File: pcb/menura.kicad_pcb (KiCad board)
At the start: 2 copper layers, 128.4 x 108.5 mm, 53 parts, among them SW1 SW_Push, SW10 SW_Push, SW11 SW_Push, SW12 SW_Push, SW13 SW_Push, SW14 SW_Push, SW15 SW_Push, SW16 SW_Push, SW17 SW_Push, SW18 SW_Push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

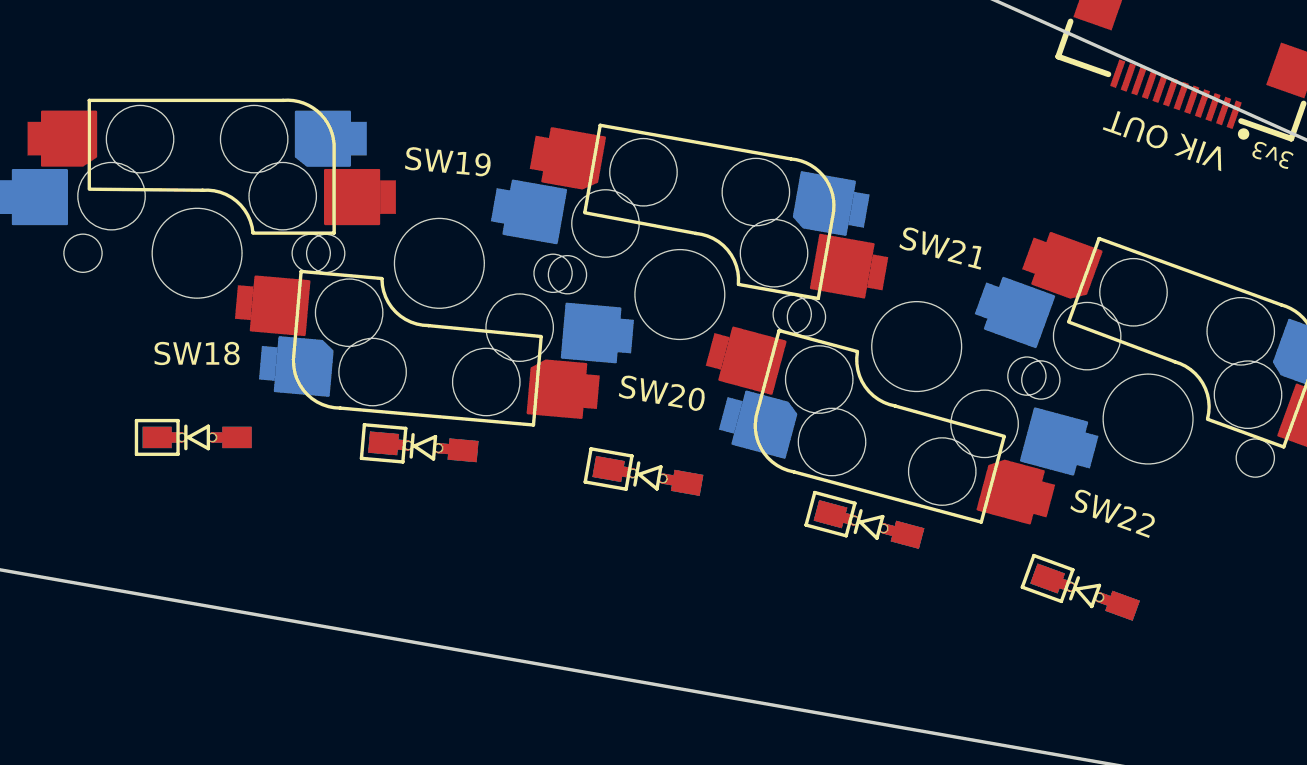
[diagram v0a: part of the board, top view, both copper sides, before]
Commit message: fix diode ordering
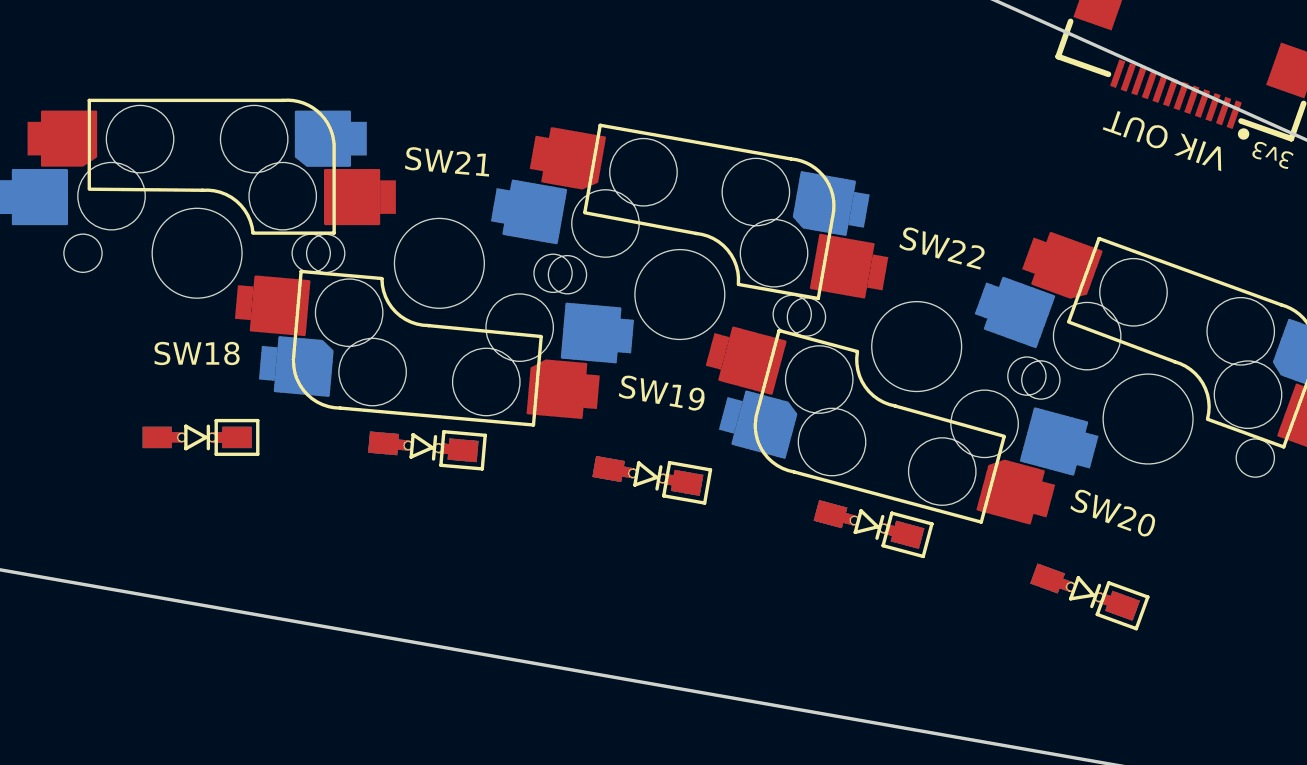
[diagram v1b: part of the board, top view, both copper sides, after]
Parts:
- moved SW21 21.6 mm to (167.8, 117.0), turned to 175 degrees
- moved SW20 21.6 mm to (199.3, 123.9), turned to -20 degrees
- moved SW19 10.8 mm to (178.5, 118.3), turned to -10 degrees
- moved SW22 10.8 mm to (189.0, 120.7), turned to 165 degrees
- turned D18 to 180 degrees
- turned D19 to 170 degrees
- turned D20 to 160 degrees
- turned D21 to 175 degrees
- turned D22 to 165 degrees
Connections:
- SW19 pad 1: col2 -> col3
- SW20 pad 1: col3 -> col4
- SW21 pad 1: col3 -> col2
- SW22 pad 1: col4 -> col3

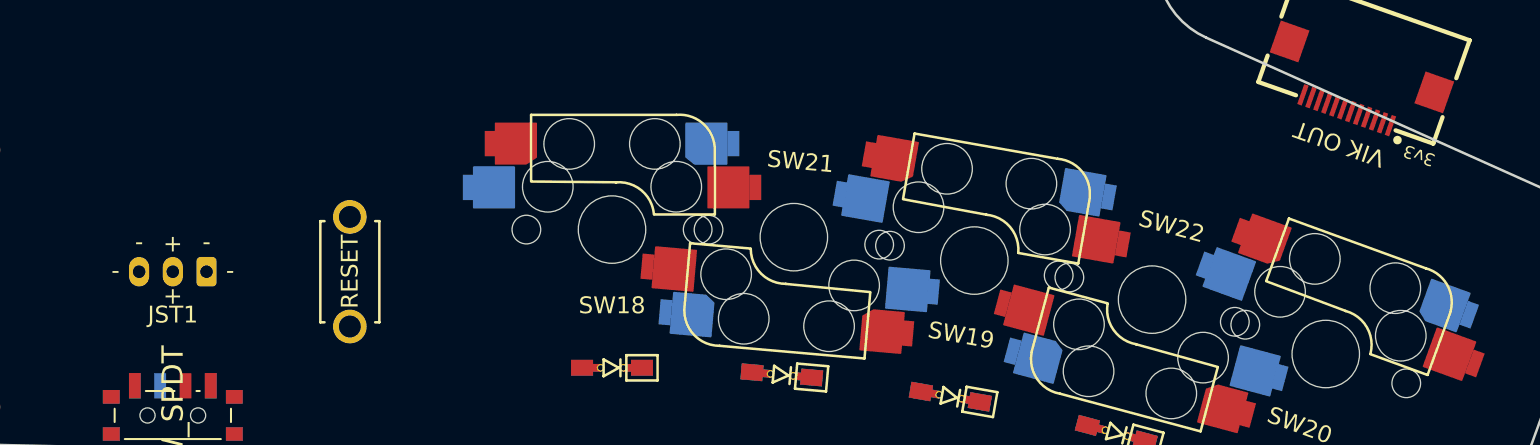
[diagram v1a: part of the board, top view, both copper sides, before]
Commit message: update footprints: centering, pad assignments
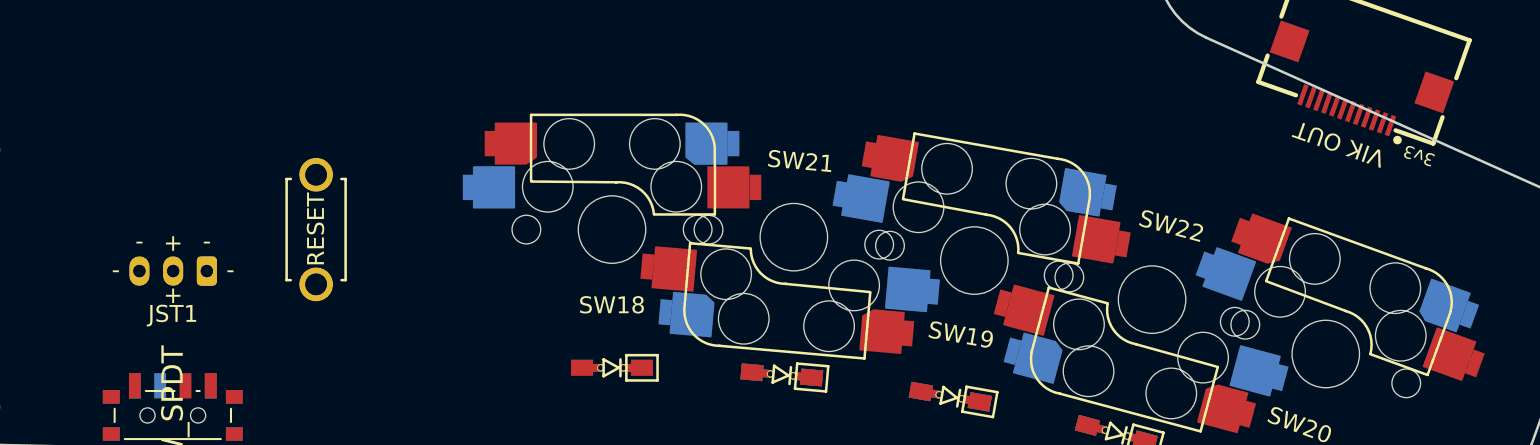
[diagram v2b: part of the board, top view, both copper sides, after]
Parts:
- moved JST1 3.20 mm to (130.9, 116.5)
- moved RSW1 3.20 mm to (139.4, 116.5)
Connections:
- MCU1 pad 10: col0 -> CS
- MCU1 pad 11: col1 -> col4
- MCU1 pad 12: col2 -> row3
- MCU1 pad 13: CS -> col3
- MCU1 pad 14: MOSI -> col2
- MCU1 pad 15: MISO -> col1
- MCU1 pad 16: SCLK -> col0
- MCU1 pad 19: col4 -> row2
- MCU1 pad 20: col3 -> row1
- MCU1 pad 7: row1 -> SCLK
- MCU1 pad 8: row2 -> MISO
- MCU1 pad 9: row3 -> MOSI

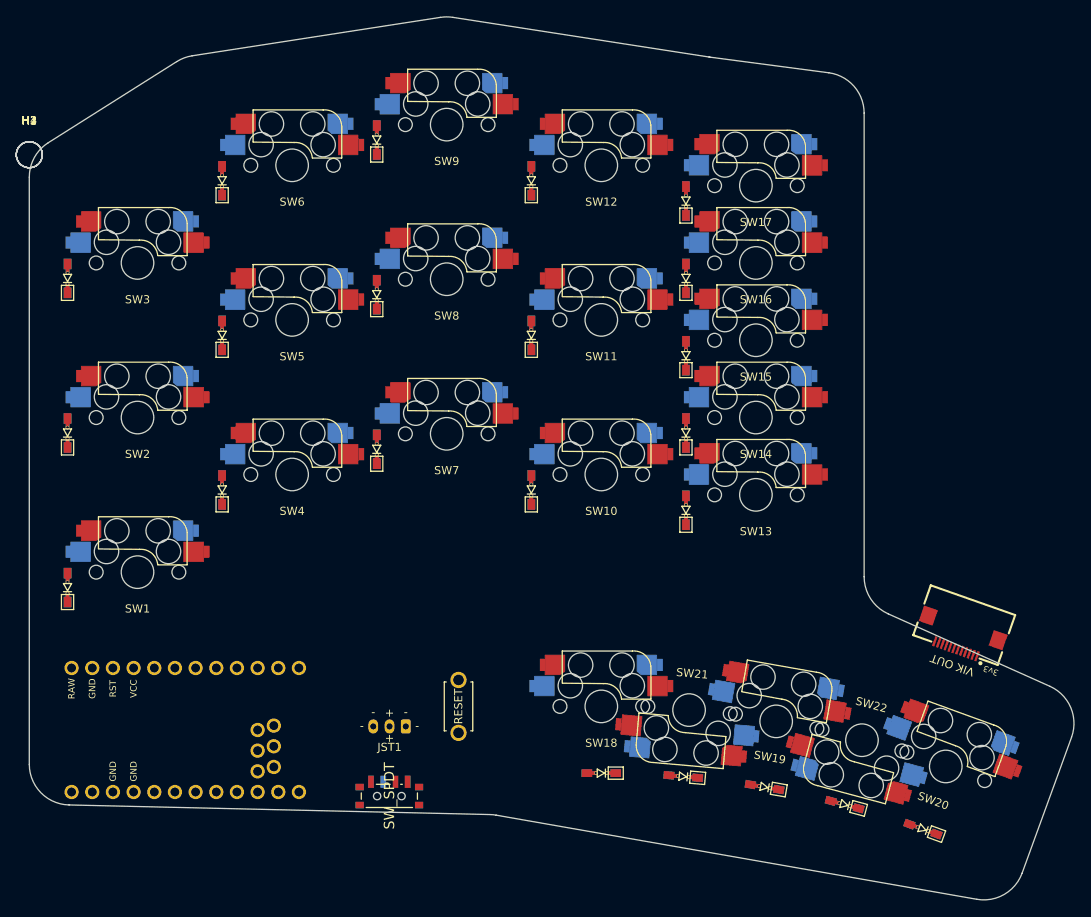
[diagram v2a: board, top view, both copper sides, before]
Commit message: iterate on power switch and jst placement
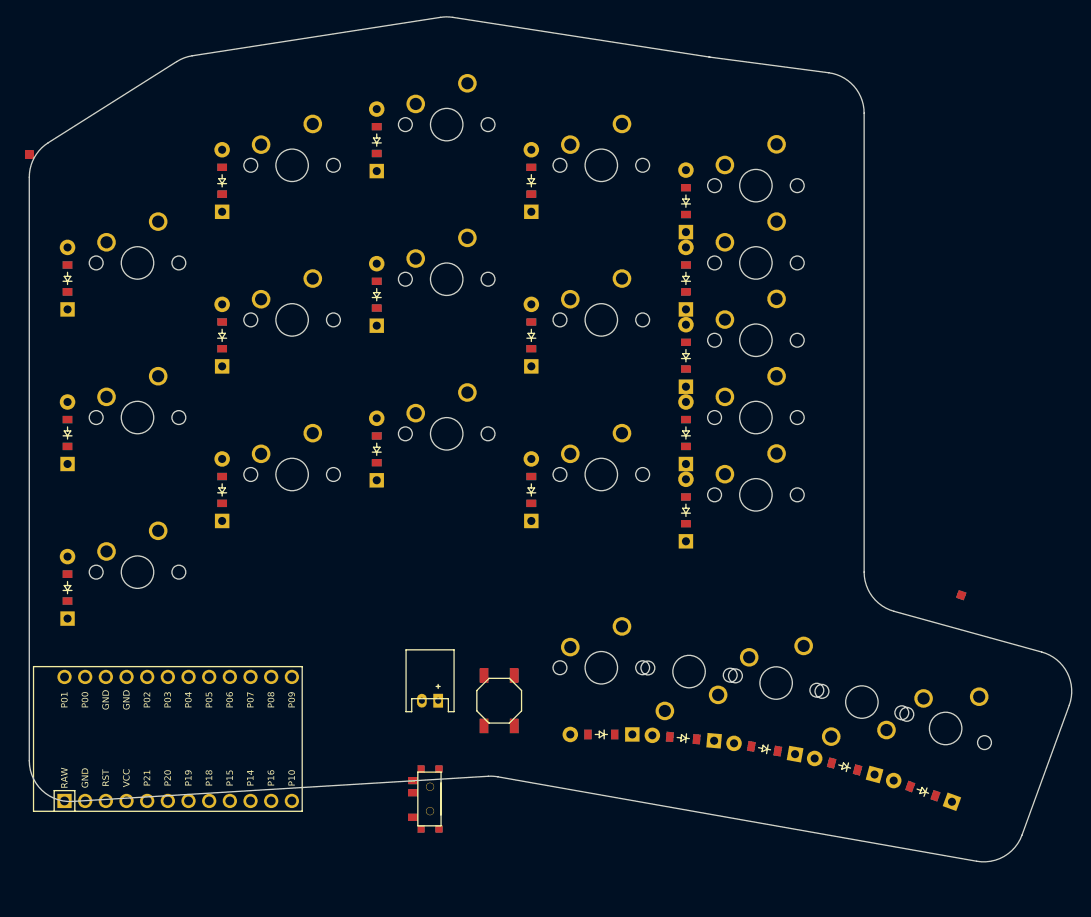
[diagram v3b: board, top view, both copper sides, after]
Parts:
- D1, D10, D11, D12, D13, D14, D15, D16, D17, D18, D19, D2, D20, D21, D22, D3, D4, D5, D6, D7, D8, D9: value 1N4148W -> (none); footprint quappo:Diode_SMD-reversible-urchin -> ComboDiode
- H1, H2, H3, H4: value MountingHole -> (none); footprint MountingHole:MountingHole_3.2mm_M3 -> SMDPad
- JST1: value Conn_01x03_Socket -> (none); footprint quappo:Connector_JST-PH-3prong -> JST_PH_S2B-PH-K_02x2.00mm_Angled
- MCU1: value N!N -> (none); footprint quappo:MCU_nice-nano -> ProMicro
- PWR1: value SW_SPDT -> (none); footprint quappo:Switch_power-reversible-kim -> E73:SPDT_C128955
- RSW1: value SW_Push -> (none); footprint quappo:Switch_reset-2pin -> E73:SW_TACT_ALPS_SKQGABE010
- SW1, SW10, SW11, SW12, SW13, SW14, SW15, SW16, SW17, SW18, SW19, SW2, SW20, SW21, SW22, SW3, SW4, SW5, SW6, SW7, SW8, SW9: value SW_Push -> (none); footprint quappo:Switch_MX-hotswap-reversible -> MX
- VIK1: value ~ -> (none); footprint quappo:Connector_vik-keyboard-horizontal -> SMDPad
- moved JST1 5.05 mm to (135.9, 115.8)
- moved RSW1 5.05 mm to (144.4, 115.8)
- moved PWR1 5.01 mm to (135.9, 127.9)
- moved D18 4.75 mm to (157.0, 120.0)
- moved SW18 4.75 mm to (157.0, 111.8)
- moved D21 4.73 mm to (167.1, 120.4)
- moved SW21 4.73 mm to (167.8, 112.2)
- moved SW19 4.71 mm to (178.5, 113.6)
- moved D19 4.71 mm to (177.1, 121.7)
- moved D22 4.69 mm to (186.9, 123.9)
- moved SW22 4.69 mm to (189.0, 116.0)
- moved VIK1 4.67 mm to (201.2, 102.8)
- moved SW20 4.67 mm to (199.3, 119.2)
- moved D20 4.67 mm to (196.5, 126.9)
- moved MCU1 1.50 mm to (105.0, 120.5)
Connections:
- D1 pad 1: row2 -> (no net)
- D1 pad 2: Net-(D1-A) -> (no net)
- D10 pad 1: row2 -> (no net)
- D10 pad 2: Net-(D10-A) -> (no net)
- D11 pad 1: row1 -> (no net)
- D11 pad 2: Net-(D11-A) -> (no net)
- D12 pad 1: row0 -> (no net)
- D12 pad 2: Net-(D12-A) -> (no net)
- D13 pad 1: row2 -> (no net)
- D13 pad 2: Net-(D13-A) -> (no net)
- D14 pad 1: row1 -> (no net)
- D14 pad 2: Net-(D14-A) -> (no net)
- D15 pad 1: row1 -> (no net)
- D15 pad 2: Net-(D15-A) -> (no net)
- D16 pad 1: row0 -> (no net)
- D16 pad 2: Net-(D16-A) -> (no net)
- D17 pad 1: row0 -> (no net)
- D17 pad 2: Net-(D17-A) -> (no net)
- D18 pad 1: row3 -> (no net)
- D18 pad 2: Net-(D18-A) -> (no net)
- D19 pad 1: row3 -> (no net)
- D19 pad 2: Net-(D19-A) -> (no net)
- D2 pad 1: row1 -> (no net)
- D2 pad 2: Net-(D2-A) -> (no net)
- D20 pad 1: row3 -> (no net)
- D20 pad 2: Net-(D20-A) -> (no net)
- D21 pad 1: row3 -> (no net)
- D21 pad 2: Net-(D21-A) -> (no net)
- D22 pad 1: row3 -> (no net)
- D22 pad 2: Net-(D22-A) -> (no net)
- D3 pad 1: row0 -> (no net)
- D3 pad 2: Net-(D3-A) -> (no net)
- D4 pad 1: row2 -> (no net)
- D4 pad 2: Net-(D4-A) -> (no net)
- D5 pad 1: row1 -> (no net)
- D5 pad 2: Net-(D5-A) -> (no net)
- D6 pad 1: row0 -> (no net)
- D6 pad 2: Net-(D6-A) -> (no net)
- D7 pad 1: row2 -> (no net)
- D7 pad 2: Net-(D7-A) -> (no net)
- D8 pad 1: row1 -> (no net)
- D8 pad 2: Net-(D8-A) -> (no net)
- D9 pad 1: row0 -> (no net)
- D9 pad 2: Net-(D9-A) -> (no net)
- JST1 pad 1: GND -> (no net)
- JST1 pad 2: Net-(JST1-Pin_2) -> (no net)
- MCU1 pad 1: unconnected-(MCU1-006-Pad1) -> RAW
- MCU1 pad 10: CS -> P14
- MCU1 pad 11: col4 -> P16
- MCU1 pad 12: row3 -> P10
- MCU1 pad 13: col3 -> P1
- MCU1 pad 14: col2 -> P0
- MCU1 pad 15: col1 -> GND
- MCU1 pad 16: col0 -> GND
- MCU1 pad 17: VIK_GPIO2 -> P2
- MCU1 pad 18: VIK_GPIO1 -> P3
- MCU1 pad 19: row2 -> P4
- MCU1 pad 2: row0 -> GND
- MCU1 pad 20: row1 -> P5
- MCU1 pad 21: +3.3V -> P6
- MCU1 pad 22: RST -> P7
- MCU1 pad 23: GND -> P8
- MCU1 pad 24: RAW -> P9
- MCU1 pad 3: GND -> RST
- MCU1 pad 4: GND -> VCC
- MCU1 pad 5: SDA -> P21
- MCU1 pad 6: SCL -> P20
- MCU1 pad 7: SCLK -> P19
- MCU1 pad 8: MISO -> P18
- MCU1 pad 9: MOSI -> P15
- PWR1 pad 1: RAW -> (no net)
- PWR1 pad 2: Net-(JST1-Pin_2) -> (no net)
- PWR1 pad 3: unconnected-(PWR1-C-Pad3)_0 -> (no net)
- RSW1 pad 1: GND -> (no net)
- RSW1 pad 2: RST -> (no net)
- SW1 pad 1: col0 -> (no net)
- SW1 pad 2: Net-(D1-A) -> (no net)
- SW10 pad 1: col3 -> (no net)
- SW10 pad 2: Net-(D10-A) -> (no net)
- SW11 pad 1: col3 -> (no net)
- SW11 pad 2: Net-(D11-A) -> (no net)
- SW12 pad 1: col3 -> (no net)
- SW12 pad 2: Net-(D12-A) -> (no net)
- SW13 pad 1: col4 -> (no net)
- SW13 pad 2: Net-(D13-A) -> (no net)
- SW14 pad 1: col4 -> (no net)
- SW14 pad 2: Net-(D14-A) -> (no net)
- SW15 pad 1: col4 -> (no net)
- SW15 pad 2: Net-(D15-A) -> (no net)
- SW16 pad 1: col4 -> (no net)
- SW16 pad 2: Net-(D16-A) -> (no net)
- SW17 pad 1: col4 -> (no net)
- SW17 pad 2: Net-(D17-A) -> (no net)
- SW18 pad 1: col2 -> (no net)
- SW18 pad 2: Net-(D18-A) -> (no net)
- SW19 pad 1: col3 -> (no net)
- SW19 pad 2: Net-(D19-A) -> (no net)
- SW2 pad 1: col0 -> (no net)
- SW2 pad 2: Net-(D2-A) -> (no net)
- SW20 pad 1: col4 -> (no net)
- SW20 pad 2: Net-(D20-A) -> (no net)
- SW21 pad 1: col2 -> (no net)
- SW21 pad 2: Net-(D21-A) -> (no net)
- SW22 pad 1: col3 -> (no net)
- SW22 pad 2: Net-(D22-A) -> (no net)
- SW3 pad 1: col0 -> (no net)
- SW3 pad 2: Net-(D3-A) -> (no net)
- SW4 pad 1: col1 -> (no net)
- SW4 pad 2: Net-(D4-A) -> (no net)
- SW5 pad 1: col1 -> (no net)
- SW5 pad 2: Net-(D5-A) -> (no net)
- SW6 pad 1: col1 -> (no net)
- SW6 pad 2: Net-(D6-A) -> (no net)
- SW7 pad 1: col2 -> (no net)
- SW7 pad 2: Net-(D7-A) -> (no net)
- SW8 pad 1: col2 -> (no net)
- SW8 pad 2: Net-(D8-A) -> (no net)
- SW9 pad 1: col2 -> (no net)
- SW9 pad 2: Net-(D9-A) -> (no net)
- VIK1 pad 1: +3.3V -> (no net)
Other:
- board size 128.4 x 108.5 mm -> 128.1 x 103.8 mm
- net class Default added: clearance 0.2, trace_width 0.25, via_dia 0.8, via_drill 0.4

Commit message: iterate on vik placement
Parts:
- D1, D10, D11, D12, D13, D14, D15, D16, D17, D18, D19, D2, D20, D21, D22, D3, D4, D5, D6, D7, D8, D9: value (none) -> 1N4148W; footprint ComboDiode -> quappo:Diode_SMD-reversible-urchin
- H1, H2, H3, H4: value (none) -> MountingHole; footprint SMDPad -> MountingHole:MountingHole_3.2mm_M3
- JST1: value (none) -> Conn_01x03_Socket; footprint JST_PH_S2B-PH-K_02x2.00mm_Angled -> quappo:Connector_JST-PH-3prong
- MCU1: value (none) -> N!N; footprint ProMicro -> quappo:MCU_nice-nano
- PWR1: value (none) -> SW_SPDT; footprint E73:SPDT_C128955 -> quappo:Switch_power-reversible-kim
- RSW1: value (none) -> SW_Push; footprint E73:SW_TACT_ALPS_SKQGABE010 -> quappo:Switch_reset-2pin
- SW1, SW10, SW11, SW12, SW13, SW14, SW15, SW16, SW17, SW18, SW19, SW2, SW20, SW21, SW22, SW3, SW4, SW5, SW6, SW7, SW8, SW9: value (none) -> SW_Push; footprint MX -> quappo:Switch_MX-hotswap-reversible
- VIK1: value (none) -> ~; footprint SMDPad -> quappo:Connector_vik-keyboard-horizontal
- moved VIK1 8.59 mm to (192.7, 102.4), turned to 165 degrees
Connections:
- D1 pad 1: (no net) -> row2
- D1 pad 2: (no net) -> Net-(D1-A)
- D10 pad 1: (no net) -> row2
- D10 pad 2: (no net) -> Net-(D10-A)
- D11 pad 1: (no net) -> row1
- D11 pad 2: (no net) -> Net-(D11-A)
- D12 pad 1: (no net) -> row0
- D12 pad 2: (no net) -> Net-(D12-A)
- D13 pad 1: (no net) -> row2
- D13 pad 2: (no net) -> Net-(D13-A)
- D14 pad 1: (no net) -> row1
- D14 pad 2: (no net) -> Net-(D14-A)
- D15 pad 1: (no net) -> row1
- D15 pad 2: (no net) -> Net-(D15-A)
- D16 pad 1: (no net) -> row0
- D16 pad 2: (no net) -> Net-(D16-A)
- D17 pad 1: (no net) -> row0
- D17 pad 2: (no net) -> Net-(D17-A)
- D18 pad 1: (no net) -> row3
- D18 pad 2: (no net) -> Net-(D18-A)
- D19 pad 1: (no net) -> row3
- D19 pad 2: (no net) -> Net-(D19-A)
- D2 pad 1: (no net) -> row1
- D2 pad 2: (no net) -> Net-(D2-A)
- D20 pad 1: (no net) -> row3
- D20 pad 2: (no net) -> Net-(D20-A)
- D21 pad 1: (no net) -> row3
- D21 pad 2: (no net) -> Net-(D21-A)
- D22 pad 1: (no net) -> row3
- D22 pad 2: (no net) -> Net-(D22-A)
- D3 pad 1: (no net) -> row0
- D3 pad 2: (no net) -> Net-(D3-A)
- D4 pad 1: (no net) -> row2
- D4 pad 2: (no net) -> Net-(D4-A)
- D5 pad 1: (no net) -> row1
- D5 pad 2: (no net) -> Net-(D5-A)
- D6 pad 1: (no net) -> row0
- D6 pad 2: (no net) -> Net-(D6-A)
- D7 pad 1: (no net) -> row2
- D7 pad 2: (no net) -> Net-(D7-A)
- D8 pad 1: (no net) -> row1
- D8 pad 2: (no net) -> Net-(D8-A)
- D9 pad 1: (no net) -> row0
- D9 pad 2: (no net) -> Net-(D9-A)
- JST1 pad 1: (no net) -> GND
- JST1 pad 2: (no net) -> Net-(JST1-Pin_2)
- MCU1 pad 1: RAW -> unconnected-(MCU1-006-Pad1)
- MCU1 pad 10: P14 -> CS
- MCU1 pad 11: P16 -> col4
- MCU1 pad 12: P10 -> row3
- MCU1 pad 13: P1 -> col3
- MCU1 pad 14: P0 -> col2
- MCU1 pad 15: GND -> col1
- MCU1 pad 16: GND -> col0
- MCU1 pad 17: P2 -> VIK_GPIO2
- MCU1 pad 18: P3 -> VIK_GPIO1
- MCU1 pad 19: P4 -> row2
- MCU1 pad 2: GND -> row0
- MCU1 pad 20: P5 -> row1
- MCU1 pad 21: P6 -> +3.3V
- MCU1 pad 22: P7 -> RST
- MCU1 pad 23: P8 -> GND
- MCU1 pad 24: P9 -> RAW
- MCU1 pad 3: RST -> GND
- MCU1 pad 4: VCC -> GND
- MCU1 pad 5: P21 -> SDA
- MCU1 pad 6: P20 -> SCL
- MCU1 pad 7: P19 -> SCLK
- MCU1 pad 8: P18 -> MISO
- MCU1 pad 9: P15 -> MOSI
- PWR1 pad 1: (no net) -> RAW
- PWR1 pad 2: (no net) -> Net-(JST1-Pin_2)
- PWR1 pad 3: (no net) -> unconnected-(PWR1-C-Pad3)_0
- RSW1 pad 1: (no net) -> GND
- RSW1 pad 2: (no net) -> RST
- SW1 pad 1: (no net) -> col0
- SW1 pad 2: (no net) -> Net-(D1-A)
- SW10 pad 1: (no net) -> col3
- SW10 pad 2: (no net) -> Net-(D10-A)
- SW11 pad 1: (no net) -> col3
- SW11 pad 2: (no net) -> Net-(D11-A)
- SW12 pad 1: (no net) -> col3
- SW12 pad 2: (no net) -> Net-(D12-A)
- SW13 pad 1: (no net) -> col4
- SW13 pad 2: (no net) -> Net-(D13-A)
- SW14 pad 1: (no net) -> col4
- SW14 pad 2: (no net) -> Net-(D14-A)
- SW15 pad 1: (no net) -> col4
- SW15 pad 2: (no net) -> Net-(D15-A)
- SW16 pad 1: (no net) -> col4
- SW16 pad 2: (no net) -> Net-(D16-A)
- SW17 pad 1: (no net) -> col4
- SW17 pad 2: (no net) -> Net-(D17-A)
- SW18 pad 1: (no net) -> col2
- SW18 pad 2: (no net) -> Net-(D18-A)
- SW19 pad 1: (no net) -> col3
- SW19 pad 2: (no net) -> Net-(D19-A)
- SW2 pad 1: (no net) -> col0
- SW2 pad 2: (no net) -> Net-(D2-A)
- SW20 pad 1: (no net) -> col4
- SW20 pad 2: (no net) -> Net-(D20-A)
- SW21 pad 1: (no net) -> col2
- SW21 pad 2: (no net) -> Net-(D21-A)
- SW22 pad 1: (no net) -> col3
- SW22 pad 2: (no net) -> Net-(D22-A)
- SW3 pad 1: (no net) -> col0
- SW3 pad 2: (no net) -> Net-(D3-A)
- SW4 pad 1: (no net) -> col1
- SW4 pad 2: (no net) -> Net-(D4-A)
- SW5 pad 1: (no net) -> col1
- SW5 pad 2: (no net) -> Net-(D5-A)
- SW6 pad 1: (no net) -> col1
- SW6 pad 2: (no net) -> Net-(D6-A)
- SW7 pad 1: (no net) -> col2
- SW7 pad 2: (no net) -> Net-(D7-A)
- SW8 pad 1: (no net) -> col2
- SW8 pad 2: (no net) -> Net-(D8-A)
- SW9 pad 1: (no net) -> col2
- SW9 pad 2: (no net) -> Net-(D9-A)
- VIK1 pad 1: (no net) -> +3.3V
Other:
- net class Default removed
